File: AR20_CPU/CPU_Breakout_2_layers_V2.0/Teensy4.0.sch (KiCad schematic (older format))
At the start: 9 parts, among them SW1 SW_Push_Dual

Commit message: V2.0 Teensy Breakout Board
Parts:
- removed BT1: 3V cell coin, Battery:BatteryHolder_Keystone_3034_1x20mm, symbol Device:Battery_Cell
- removed Teensy4.0: Teensy_pins, Teensy_Footprint_Library:Teensy_40_footprint, symbol BreakoutBoardTeensy:Teensy_pins
- added T4: BreakoutBoardTeensy_Teensy_pins, Teensy_Footprint_Library:Teensy_40_footprint, symbol teensy4_header_breakout-cache:BreakoutBoardTeensy_Teensy_pins
- added U1: S8211-46R, Teensy_Footprint_Library:S8211-46R, symbol teensy4_header_breakout-cache:S8211-46R
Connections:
- net labels added: 20_TX3, 21_RX3, CANH, CANL, SCLK
- net labels removed: 13(LED), 20_TX5, 21_RX5
- wire segments 89 -> 91
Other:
- moved on the sheet: C18, MX1

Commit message: Edited
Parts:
- removed SW1: SW_Push_Dual, Button_Switch_SMD:SW_SPST_B3S-1000, symbol Switch:SW_Push_Dual
- added SW1: SW_Push_Dual, Button_Switch_SMD:SW_SPST_B3S-1000, symbol teensy4_header_breakout-cache:SW_Push_Dual
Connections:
- net 26_A12: now also MX1.25 (Pin_25)
- net Ground: now also SW1.1; no longer MX1.25 (Pin_25)
- net ON_OFF: now also SW1.2
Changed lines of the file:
@@
 Text GLabel 4000 5100 0    50   Input ~ 0
-Ground
-Text GLabel 4000 5000 0    50   Input ~ 0
 Ground
 Text GLabel 4000 5200 0    50   Input ~ 0
@@
 Text GLabel 4000 3300 0    50   Input ~ 0
 24_TX6_A10
-$Comp
-L Switch:SW_Push_Dual SW1
-U 1 1 5E1C0144
-P 6300 1300
-F 0 "SW1" H 5700 1350 50  0000 C CNN
-F 1 "SW_Push_Dual" H 5750 1250 50  0000 C CNN
-F 2 "Button_Switch_SMD:SW_SPST_B3S-1000" H 6300 1500 50  0001 C CNN
-F 3 "~" H 6300 1500 50  0001 C CNN
-	1    6300 1300
-	1    0    0    -1
-$EndComp
-Wire Wire Line
-	6100 1650 6300 1650
-Wire Wire Line
-	6100 1500 6100 1650
-Wire Wire Line
-	6500 1000 6500 1300
-Wire Wire Line
-	6300 1000 6500 1000
-Connection ~ 6100 1500
-Wire Wire Line
-	6100 1300 6100 1500
-Connection ~ 6500 1300
-Wire Wire Line
-	6500 1300 6500 1500
 Text GLabel 4000 6100 0    50   Input ~ 0
 CANH
@@
 	7900 1450 7900 1250
 Connection ~ 7900 1250
+Wire Wire Line
+	6300 1000 6300 1100
+Wire Wire Line
+	6300 1100 6500 1100
+Wire Wire Line
+	6500 1100 6500 1300
+Wire Wire Line
+	6500 1300 6500 1500
+Connection ~ 6500 1300
+Wire Wire Line
+	6100 1300 6100 1500
+Wire Wire Line
+	6100 1500 6100 1650
+Wire Wire Line
+	6100 1650 6300 1650
+Connection ~ 6100 1500
+$Comp
+L teensy4_header_breakout-cache:SW_Push_Dual SW1
+U 1 1 5E659C41
+P 6300 1300
+F 0 "SW1" H 6300 1585 50  0000 C CNN
+F 1 "SW_Push_Dual" H 6300 1494 50  0000 C CNN
+F 2 "Button_Switch_SMD:SW_SPST_B3S-1000" H 6300 1500 50  0001 C CNN
+F 3 "~" H 6300 1500 50  0001 C CNN
+	1    6300 1300
+	1    0    0    -1
+$EndComp
+Text GLabel 4000 5000 0    50   Input ~ 0
+26_A12
 $EndSCHEMATC

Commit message: Push button edited
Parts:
- removed SW1: SW_Push_Dual, Button_Switch_SMD:SW_SPST_B3S-1000, symbol teensy4_header_breakout-cache:SW_Push_Dual
- added SW1, SW2: SW_Push, Button_Switch_SMD:SW_SPST_B3U-1000P, symbol Switch:SW_Push
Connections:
- net Ground: now also SW1.2, SW2.2
- net ON_OFF: now also SW2.1
- net Program: now reaches T4.32 (PROGRAM)
- net Program: now also SW1.1
- no-connect marks 1 -> 0
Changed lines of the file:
@@
 Text GLabel 9150 3350 2    50   Input ~ 0
 Out4
-NoConn ~ 9150 4250
 Text GLabel 6800 4550 0    50   Input ~ 0
 26_A12
@@
 Text GLabel 6800 2750 0    50   Input ~ 0
 Ground
-Text GLabel 6300 1650 3    50   Input ~ 0
+Text GLabel 5800 1000 3    50   Input ~ 0
 Ground
-Text GLabel 6300 1000 1    50   Input ~ 0
+Text GLabel 5000 1000 1    50   Input ~ 0
 ON_OFF
 Text GLabel 7900 1000 1    50   Input ~ 0
@@
 	7900 1450 7900 1250
 Connection ~ 7900 1250
+Text GLabel 4000 5000 0    50   Input ~ 0
+26_A12
+$Comp
+L Switch:SW_Push SW2
+U 1 1 5E64113F
+P 5400 1000
+F 0 "SW2" H 5400 1285 50  0000 C CNN
+F 1 "SW_Push" H 5400 1194 50  0000 C CNN
+F 2 "Button_Switch_SMD:SW_SPST_B3U-1000P" H 5400 1200 50  0001 C CNN
+F 3 "~" H 5400 1200 50  0001 C CNN
+	1    5400 1000
+	1    0    0    -1
+$EndComp
 Wire Wire Line
-	6300 1000 6300 1100
-Wire Wire Line
-	6300 1100 6500 1100
-Wire Wire Line
-	6500 1100 6500 1300
-Wire Wire Line
-	6500 1300 6500 1500
-Connection ~ 6500 1300
-Wire Wire Line
-	6100 1300 6100 1500
-Wire Wire Line
-	6100 1500 6100 1650
+	5600 1000 5800 1000
 Wire Wire Line
-	6100 1650 6300 1650
-Connection ~ 6100 1500
+	5200 1000 5000 1000
+Text GLabel 4200 1000 3    50   Input ~ 0
+Ground
 $Comp
-L teensy4_header_breakout-cache:SW_Push_Dual SW1
-U 1 1 5E659C41
-P 6300 1300
-F 0 "SW1" H 6300 1585 50  0000 C CNN
-F 1 "SW_Push_Dual" H 6300 1494 50  0000 C CNN
-F 2 "Button_Switch_SMD:SW_SPST_B3S-1000" H 6300 1500 50  0001 C CNN
-F 3 "~" H 6300 1500 50  0001 C CNN
-	1    6300 1300
+L Switch:SW_Push SW1
+U 1 1 5E657BDB
+P 3800 1000
+F 0 "SW1" H 3800 1285 50  0000 C CNN
+F 1 "SW_Push" H 3800 1194 50  0000 C CNN
+F 2 "Button_Switch_SMD:SW_SPST_B3U-1000P" H 3800 1200 50  0001 C CNN
+F 3 "~" H 3800 1200 50  0001 C CNN
+	1    3800 1000
 	1    0    0    -1
 $EndComp
-Text GLabel 4000 5000 0    50   Input ~ 0
-26_A12
+Wire Wire Line
+	4000 1000 4200 1000
+Wire Wire Line
+	3600 1000 3400 1000
+Text GLabel 9150 4250 2    50   Input ~ 0
+Program
+Text GLabel 3400 1000 1    50   Input ~ 0
+Program
 $EndSCHEMATC

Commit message: Edited
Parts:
- added C13: 10u, Capacitor_SMD:C_0603_1608Metric, symbol Device:C
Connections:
- net Ground: now also C13.1
- net Vinn_5V: now also C13.2
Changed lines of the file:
@@
 Text GLabel 3400 1000 1    50   Input ~ 0
 Program
+Text GLabel 3300 2200 2    50   Input ~ 0
+Ground
+$Comp
+L Device:C C13
+U 1 1 5E64746B
+P 3300 2350
+F 0 "C13" H 3415 2396 50  0000 L CNN
+F 1 "10u" H 3415 2305 50  0000 L CNN
+F 2 "Capacitor_SMD:C_0603_1608Metric" H 3338 2200 50  0001 C CNN
+F 3 "~" H 3300 2350 50  0001 C CNN
+	1    3300 2350
+	1    0    0    -1
+$EndComp
+Text GLabel 3300 2650 0    50   Input ~ 0
+Vinn_5V
+Wire Wire Line
+	3300 2500 3300 2650
 $EndSCHEMATC

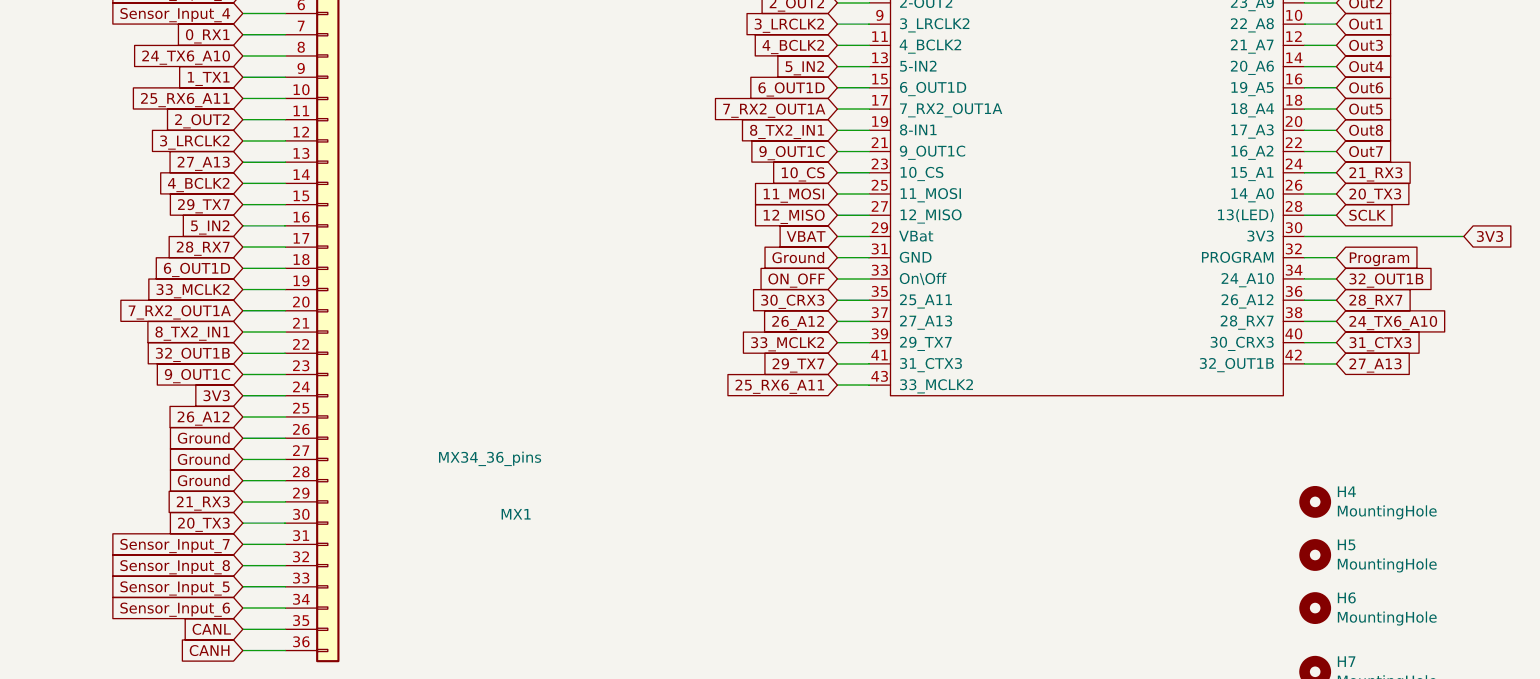
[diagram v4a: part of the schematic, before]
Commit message: Endret SCLK pin til SD
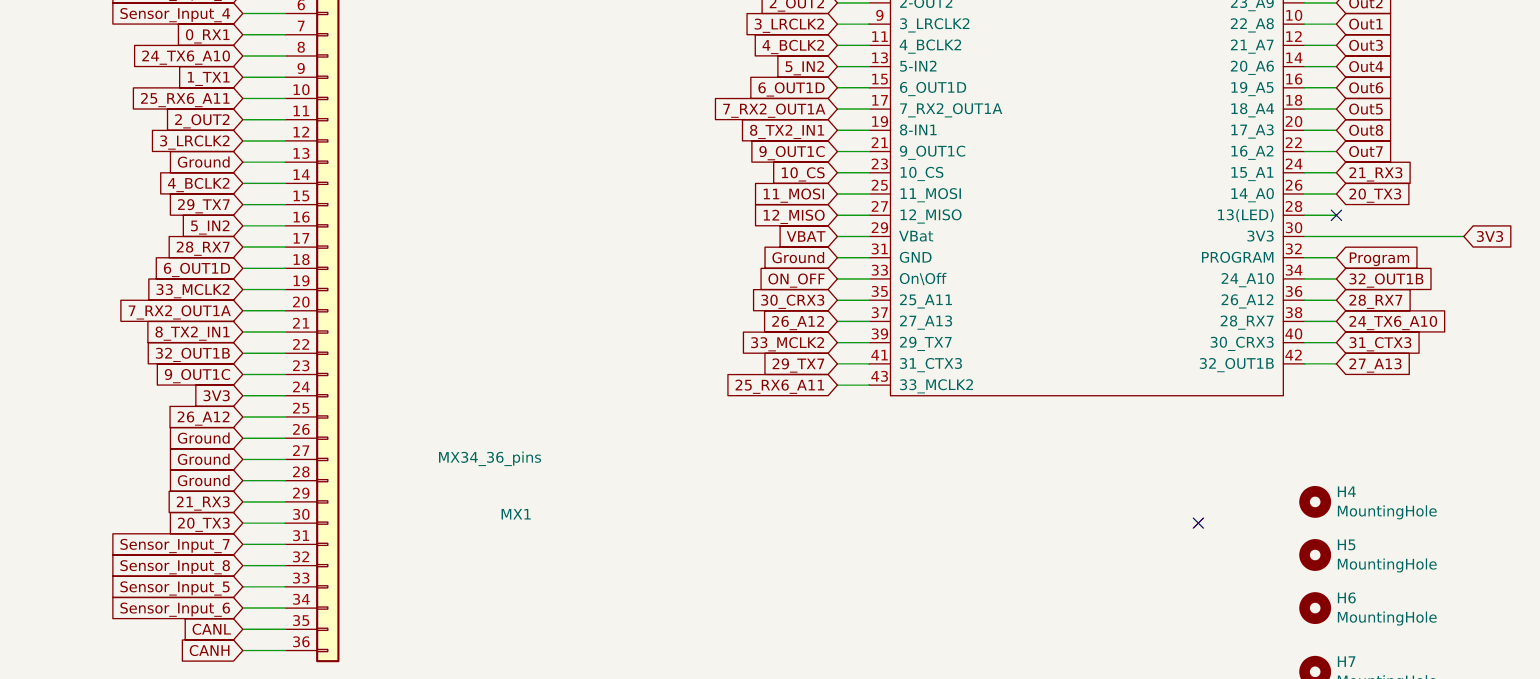
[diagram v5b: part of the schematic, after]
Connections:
- net 27_A13: no longer MX1.13 (Pin_13)
- net Ground: now also MX1.13 (Pin_13)
- net SCLK: no longer names the net of T4.28 (13(LED))
- no-connect marks 0 -> 2
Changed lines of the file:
@@
 Text GLabel 9150 2950 2    50   Input ~ 0
 3.3V
-Text GLabel 9150 4050 2    50   Input ~ 0
-SCLK
 Text GLabel 9150 2750 2    50   Input ~ 0
 Vinn_5V
@@
 Text GLabel 4000 4000 0    50   Input ~ 0
 29_TX7
-Text GLabel 4000 3800 0    50   Input ~ 0
-27_A13
 Text GLabel 4000 4800 0    50   Input ~ 0
 9_OUT1C
@@
 Wire Wire Line
 	3300 2500 3300 2650
+NoConn ~ 9150 4050
+NoConn ~ 8500 5500
+Text GLabel 4000 3800 0    50   Input ~ 0
+Ground
 $EndSCHEMATC
